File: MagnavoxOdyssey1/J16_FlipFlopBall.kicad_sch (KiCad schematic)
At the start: 15 parts

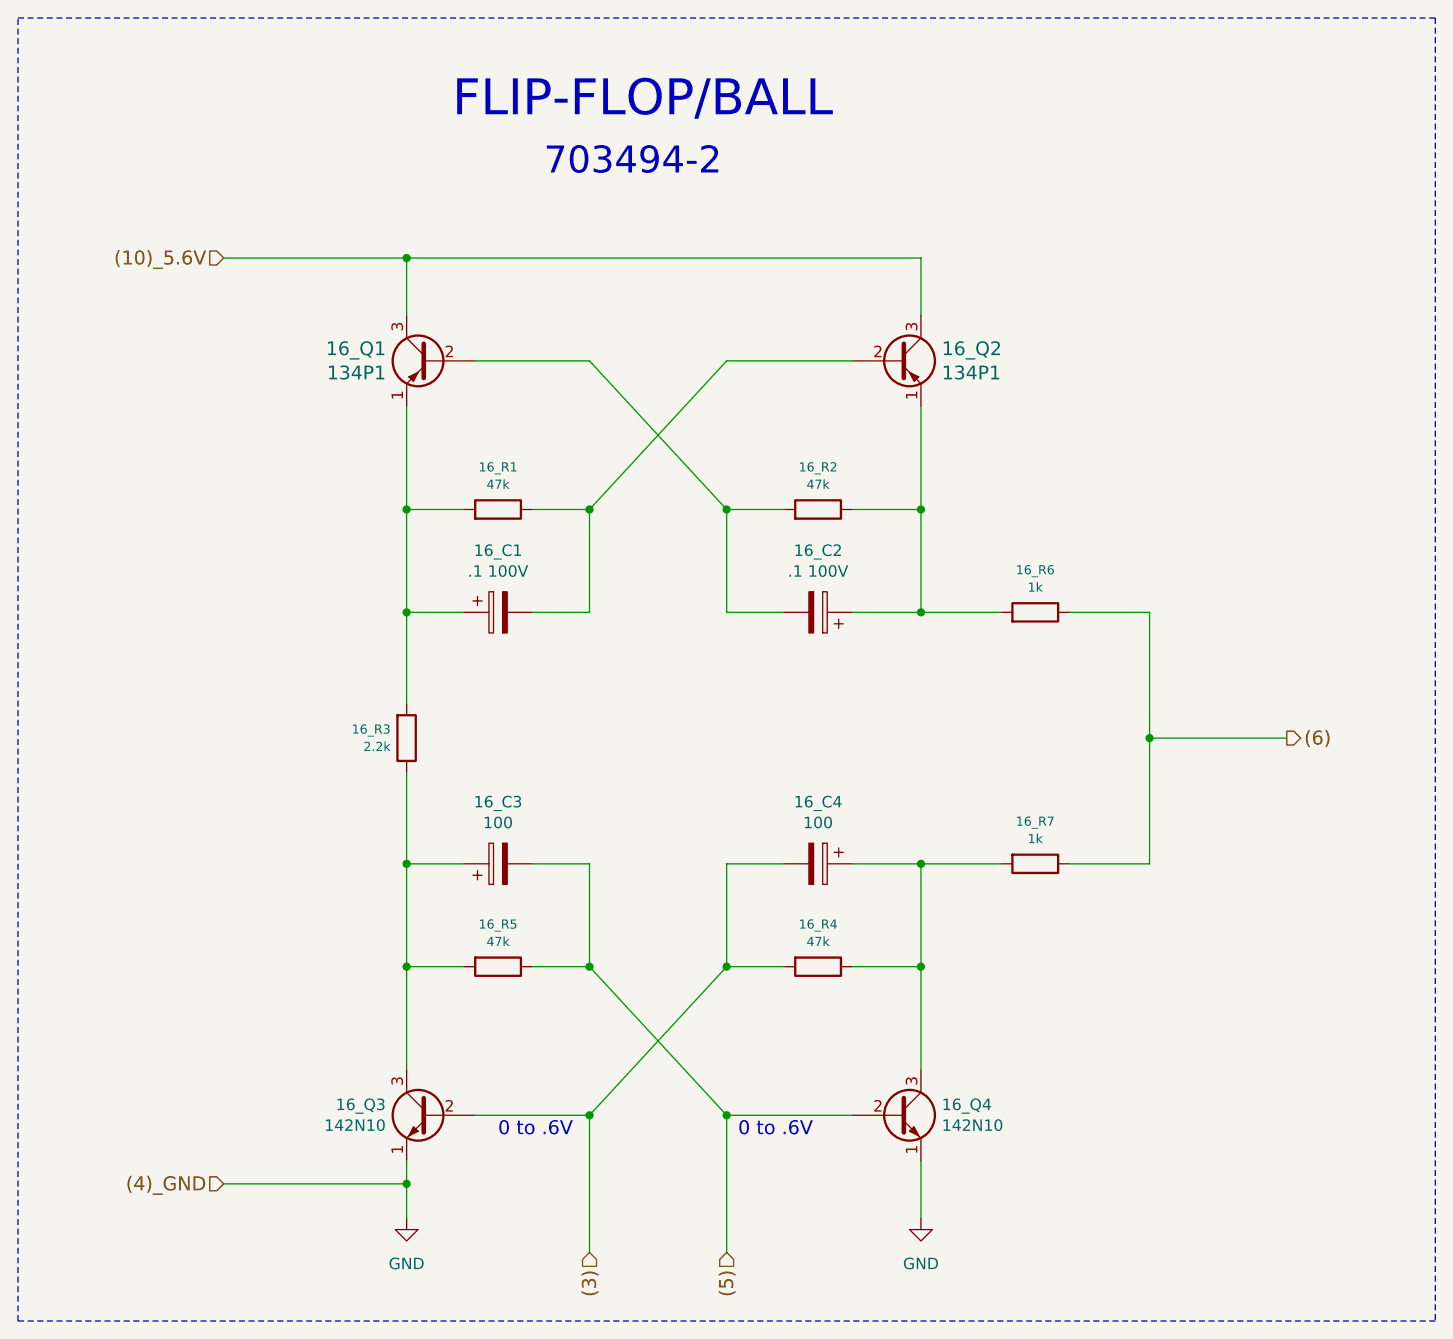
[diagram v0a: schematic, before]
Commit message: update to kicad 9
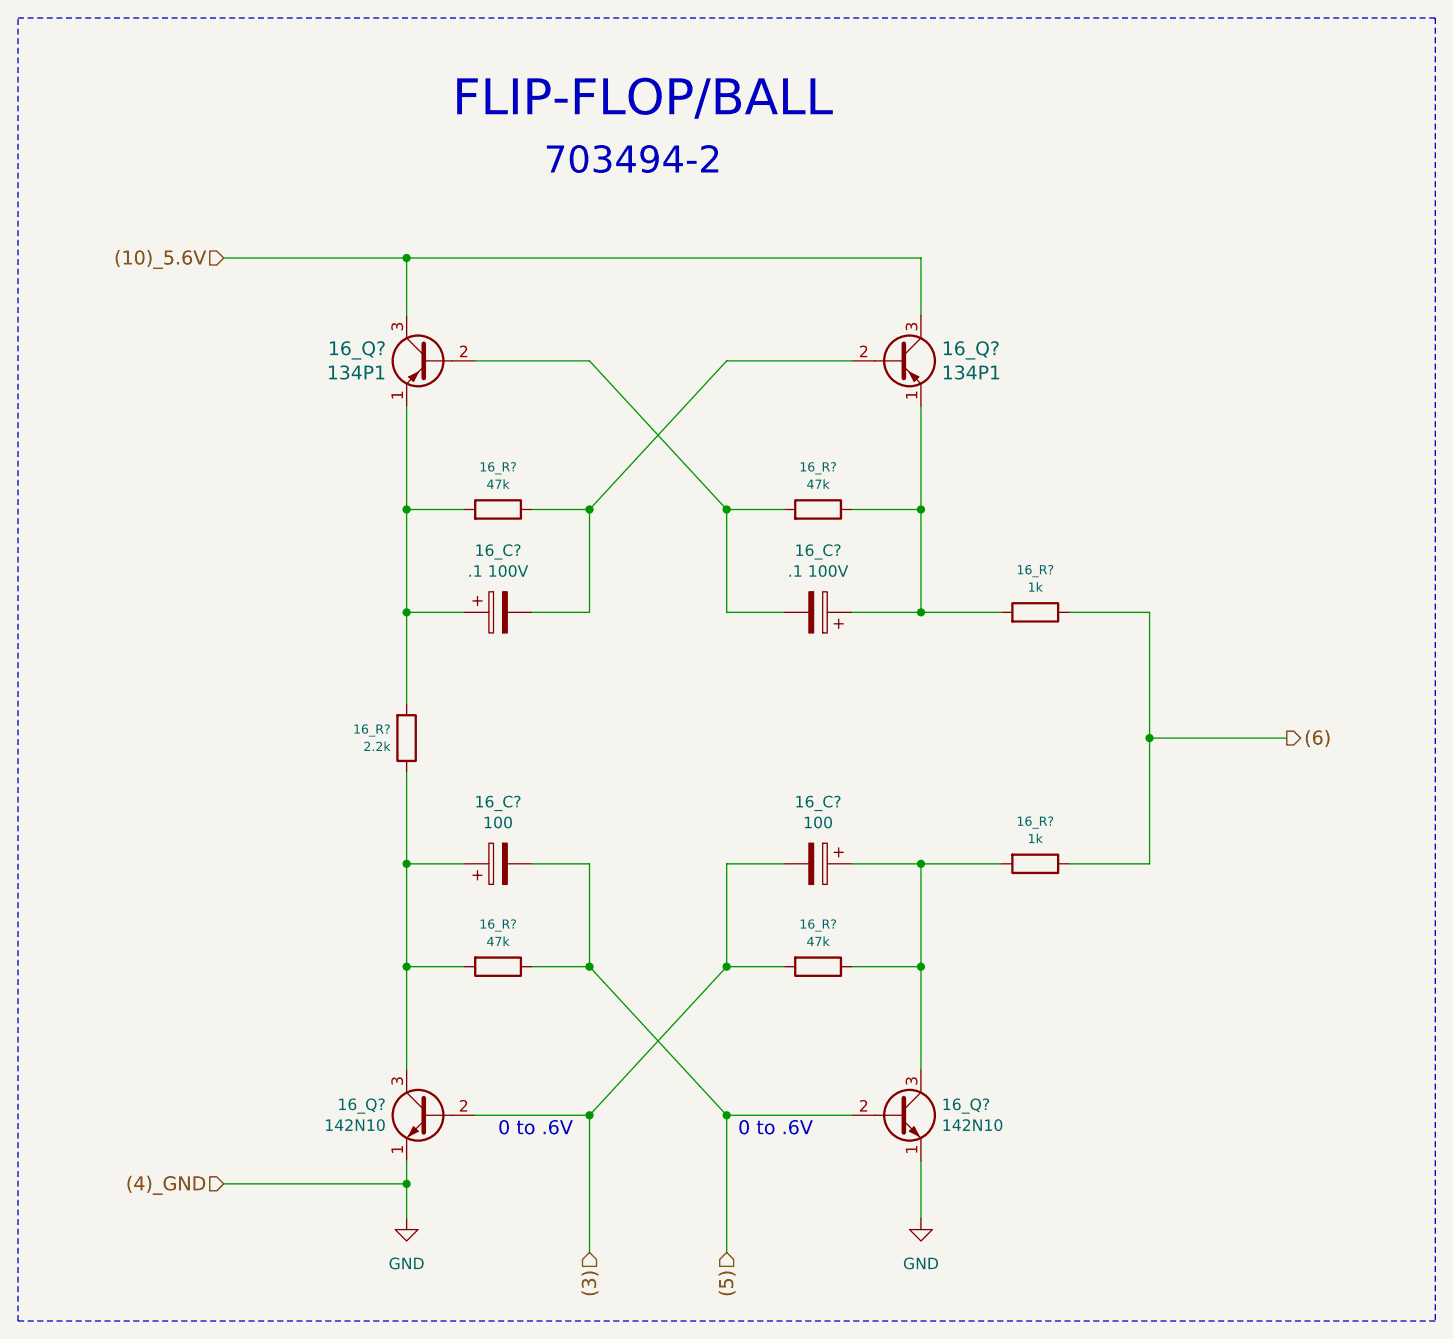
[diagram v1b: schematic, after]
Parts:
- 16_Q?: renamed from 16_Q4; symbol Device:Q_NPN_EBC -> Transistor_BJT:Q_NPN_EBC
- 16_Q?: renamed from 16_Q3; symbol Device:Q_NPN_EBC -> Transistor_BJT:Q_NPN_EBC
- 16_Q?: renamed from 16_Q2; symbol Device:Q_PNP_EBC -> Transistor_BJT:Q_PNP_EBC
- 16_Q?: renamed from 16_Q1; symbol Device:Q_PNP_EBC -> Transistor_BJT:Q_PNP_EBC
- renumbered 16_C3 to 16_C?, 16_C4 to 16_C?, 16_C1 to 16_C?, 16_C2 to 16_C?, 16_R4 to 16_R?, 16_R5 to 16_R?, 16_R7 to 16_R?, 16_R2 to 16_R?, 16_R1 to 16_R?, 16_R6 to 16_R?, 16_R3 to 16_R?
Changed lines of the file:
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@@
 (kicad_sch
-	(version 20231120)
+	(version 20250114)
 	(generator "eeschema")
-	(generator_version "8.0")
+	(generator_version "9.0")
 	(paper "A4")
+	(text "0 to .6V"
+		(exclude_from_sim no)
+		(at 116.84 140.97 0)
+		(effects
+			(font
+				(size 1.5494 1.5494)
+			)
+			(justify left bottom)
+		)
+	)
+	(text "0 to .6V"
+		(exclude_from_sim no)
+		(at 143.51 140.97 0)
+		(effects
+			(font
+				(size 1.5494 1.5494)
+			)
+			(justify left bottom)
+		)
+	)
+	(text "FLIP-FLOP/BALL"
+		(exclude_from_sim no)
+		(at 111.76 27.94 0)
+		(effects
+			(font
+				(size 3.9878 3.9878)
+			)
+			(justify left bottom)
+		)
+	)
+	(text "703494-2"
+		(exclude_from_sim no)
+		(at 121.92 34.29 0)
+		(effects
+			(font
+				(size 2.9972 2.9972)
+			)
+			(justify left bottom)
+		)
+	)
 	(junction
 		(at 142.24 71.12)
@@
 			(width 0)
 			(type default)
-		)
-	)
-	(text "0 to .6V"
-		(exclude_from_sim no)
-		(at 116.84 140.97 0)
-		(effects
-			(font
-				(size 1.5494 1.5494)
-			)
-			(justify left bottom)
-		)
-	)
-	(text "0 to .6V"
-		(exclude_from_sim no)
-		(at 143.51 140.97 0)
-		(effects
-			(font
-				(size 1.5494 1.5494)
-			)
-			(justify left bottom)
-		)
-	)
-	(text "FLIP-FLOP/BALL"
-		(exclude_from_sim no)
-		(at 111.76 27.94 0)
-		(effects
-			(font
-				(size 3.9878 3.9878)
-			)
-			(justify left bottom)
-		)
-	)
-	(text "703494-2"
-		(exclude_from_sim no)
-		(at 121.92 34.29 0)
-		(effects
-			(font
-				(size 2.9972 2.9972)
-			)
-			(justify left bottom)
 		)
 	)
@@
 	)
 	(symbol
-		(lib_id "Device:Q_NPN_EBC")
+		(lib_id "Transistor_BJT:Q_NPN_EBC")
 		(at 161.29 138.43 0)
 		(unit 1)
@@
 		(on_board yes)
 		(dnp no)
-		(property "Reference" "16_Q4"
+		(property "Reference" "16_Q?"
 			(at 166.1414 137.2616 0)
 			(effects
@@
 		(pin "3"
 		)
+		(instances
+			(project "MagnavoxOdyssey1"
+				(path "/adb6e295-eae5-402e-a614-02a705c3e27c/00000000-0000-0000-0000-0000588fbf2a"
+					(reference "16_Q?")
+					(unit 1)
+				)
+			)
+		)
 	)
 	(symbol
-		(lib_id "Device:Q_NPN_EBC")
+		(lib_id "Transistor_BJT:Q_NPN_EBC")
 		(at 109.22 138.43 0)
 		(mirror y)
@@
 		(on_board yes)
 		(dnp no)
-		(property "Reference" "16_Q3"
+		(property "Reference" "16_Q?"
 			(at 104.3686 137.2616 0)
 			(effects
@@
 		)
 		(pin "3"
+		)
+		(instances
+			(project "MagnavoxOdyssey1"
+				(path "/adb6e295-eae5-402e-a614-02a705c3e27c/00000000-0000-0000-0000-0000588fbf2a"
+					(reference "16_Q?")
+					(unit 1)
+				)
+			)
 		)
 	)
@@
 		(on_board yes)
 		(dnp no)
-		(property "Reference" "16_R4"
+		(property "Reference" "16_R?"
 			(at 152.4 117.221 90)
 			(effects
@@
 		)
 		(pin "2"
+		)
+		(instances
+			(project "MagnavoxOdyssey1"
+				(path "/adb6e295-eae5-402e-a614-02a705c3e27c/00000000-0000-0000-0000-0000588fbf2a"
+					(reference "16_R?")
+					(unit 1)
+				)
+			)
 		)
 	)
@@
 		(on_board yes)
 		(dnp no)
-		(property "Reference" "16_R5"
+		(property "Reference" "16_R?"
 			(at 116.84 117.221 90)
 			(effects
@@
 		)
 		(pin "2"
+		)
+		(instances
+			(project "MagnavoxOdyssey1"
+				(path "/adb6e295-eae5-402e-a614-02a705c3e27c/00000000-0000-0000-0000-0000588fbf2a"
+					(reference "16_R?")
+					(unit 1)
+				)
+			)
 		)
 	)
@@
 		(on_board yes)
 		(dnp no)
-		(property "Reference" "16_C3"
+		(property "Reference" "16_C?"
 			(at 116.84 103.632 90)
 			(effects
@@
 		)
 		(pin "2"
+		)
+		(instances
+			(project "MagnavoxOdyssey1"
+				(path "/adb6e295-eae5-402e-a614-02a705c3e27c/00000000-0000-0000-0000-0000588fbf2a"
+					(reference "16_C?")
+					(unit 1)
+				)
+			)
 		)
 	)
@@
 		(on_board yes)
 		(dnp no)
-		(property "Reference" "16_C4"
+		(property "Reference" "16_C?"
 			(at 152.4 103.632 90)
 			(effects
@@
 		)
 		(pin "2"
+		)
+		(instances
+			(project "MagnavoxOdyssey1"
+				(path "/adb6e295-eae5-402e-a614-02a705c3e27c/00000000-0000-0000-0000-0000588fbf2a"
+					(reference "16_C?")
+					(unit 1)
+				)
+			)
 		)
 	)
@@
 		(on_board yes)
 		(dnp no)
-		(property "Reference" "16_R7"
+		(property "Reference" "16_R?"
 			(at 176.53 105.791 90)
 			(effects
@@
 		)
 		(pin "1"
+		)
+		(instances
+			(project "MagnavoxOdyssey1"
+				(path "/adb6e295-eae5-402e-a614-02a705c3e27c/00000000-0000-0000-0000-0000588fbf2a"
+					(reference "16_R?")
+					(unit 1)
+				)
+			)
 		)
 	)
@@
 		(on_board yes)
 		(dnp no)
-		(property "Reference" "16_R2"
+		(property "Reference" "16_R?"
 			(at 152.4 66.421 90)
 			(effects
@@
 		)
 		(pin "2"
+		)
+		(instances
+			(project "MagnavoxOdyssey1"
+				(path "/adb6e295-eae5-402e-a614-02a705c3e27c/00000000-0000-0000-0000-0000588fbf2a"
+					(reference "16_R?")
+					(unit 1)
+				)
+			)
 		)
 	)
@@
 		(on_board yes)
 		(dnp no)
-		(property "Reference" "16_R1"
+		(property "Reference" "16_R?"
 			(at 116.84 66.421 90)
 			(effects
@@
 		)
 		(pin "2"
+		)
+		(instances
+			(project "MagnavoxOdyssey1"
+				(path "/adb6e295-eae5-402e-a614-02a705c3e27c/00000000-0000-0000-0000-0000588fbf2a"
+					(reference "16_R?")
+					(unit 1)
+				)
+			)
 		)
 	)
@@
 		(on_board yes)
 		(dnp no)
-		(property "Reference" "16_C1"
+		(property "Reference" "16_C?"
 			(at 116.84 75.692 90)
 			(effects
@@
 		)
 		(pin "2"
+		)
+		(instances
+			(project "MagnavoxOdyssey1"
+				(path "/adb6e295-eae5-402e-a614-02a705c3e27c/00000000-0000-0000-0000-0000588fbf2a"
+					(reference "16_C?")
+					(unit 1)
+				)
+			)
 		)
 	)
@@
 		(on_board yes)
 		(dnp no)
-		(property "Reference" "16_C2"
+		(property "Reference" "16_C?"
 			(at 152.4 75.692 90)
 			(effects
@@
 		)
 		(pin "2"
+		)
+		(instances
+			(project "MagnavoxOdyssey1"
+				(path "/adb6e295-eae5-402e-a614-02a705c3e27c/00000000-0000-0000-0000-0000588fbf2a"
+					(reference "16_C?")
+					(unit 1)
+				)
+			)
 		)
 	)
@@
 		(on_board yes)
 		(dnp no)
-		(property "Reference" "16_R6"
+		(property "Reference" "16_R?"
 			(at 176.53 77.851 90)
 			(effects
@@
 		)
 		(pin "2"
+		)
+		(instances
+			(project "MagnavoxOdyssey1"
+				(path "/adb6e295-eae5-402e-a614-02a705c3e27c/00000000-0000-0000-0000-0000588fbf2a"
+					(reference "16_R?")
+					(unit 1)
+				)
+			)
 		)
 	)
@@
 		(on_board yes)
 		(dnp no)
-		(property "Reference" "16_R3"
+		(property "Reference" "16_R?"
 			(at 104.902 95.5548 0)
 			(effects
@@
 		(pin "2"
 		)
+		(instances
+			(project "MagnavoxOdyssey1"
+				(path "/adb6e295-eae5-402e-a614-02a705c3e27c/00000000-0000-0000-0000-0000588fbf2a"
+					(reference "16_R?")
+					(unit 1)
+				)
+			)
+		)
 	)
 	(symbol
-		(lib_id "Device:Q_PNP_EBC")
+		(lib_id "Transistor_BJT:Q_PNP_EBC")
 		(at 161.29 54.61 0)
 		(unit 1)
@@
 		(on_board yes)
 		(dnp no)
-		(property "Reference" "16_Q2"
+		(property "Reference" "16_Q?"
 			(at 166.1414 53.2638 0)
 			(effects
@@
 		(pin "3"
 		)
+		(instances
+			(project "MagnavoxOdyssey1"
+				(path "/adb6e295-eae5-402e-a614-02a705c3e27c/00000000-0000-0000-0000-0000588fbf2a"
+					(reference "16_Q?")
+					(unit 1)
+				)
+			)
+		)
 	)
 	(symbol
-		(lib_id "Device:Q_PNP_EBC")
+		(lib_id "Transistor_BJT:Q_PNP_EBC")
 		(at 109.22 54.61 0)
 		(mirror y)
@@
 		(on_board yes)
 		(dnp no)
-		(property "Reference" "16_Q1"
+		(property "Reference" "16_Q?"
 			(at 104.394 53.2638 0)
 			(effects
@@
 		(pin "3"
 		)
-	)
+		(instances
+			(project "MagnavoxOdyssey1"
+				(path "/adb6e295-eae5-402e-a614-02a705c3e27c/00000000-0000-0000-0000-0000588fbf2a"
+					(reference "16_Q?")
+					(unit 1)
+				)
+			)
+		)
+	)

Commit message: annotate
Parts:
- gave numbers to parts that had none: 15
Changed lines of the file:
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@@
 		(on_board yes)
 		(dnp no)
-		(property "Reference" "16_Q?"
+		(property "Reference" "16_Q4"
 			(at 166.1414 137.2616 0)
 			(effects
@@
 			(project "MagnavoxOdyssey1"
 				(path "/adb6e295-eae5-402e-a614-02a705c3e27c/00000000-0000-0000-0000-0000588fbf2a"
-					(reference "16_Q?")
+					(reference "16_Q4")
 					(unit 1)
 				)
@@
 		(on_board yes)
 		(dnp no)
-		(property "Reference" "16_Q?"
+		(property "Reference" "16_Q3"
 			(at 104.3686 137.2616 0)
 			(effects
@@
 			(project "MagnavoxOdyssey1"
 				(path "/adb6e295-eae5-402e-a614-02a705c3e27c/00000000-0000-0000-0000-0000588fbf2a"
-					(reference "16_Q?")
+					(reference "16_Q3")
 					(unit 1)
 				)
@@
 		(on_board yes)
 		(dnp no)
-		(property "Reference" "16_R?"
+		(property "Reference" "16_R7"
 			(at 152.4 117.221 90)
 			(effects
@@
 			(project "MagnavoxOdyssey1"
 				(path "/adb6e295-eae5-402e-a614-02a705c3e27c/00000000-0000-0000-0000-0000588fbf2a"
-					(reference "16_R?")
+					(reference "16_R7")
 					(unit 1)
 				)
@@
 		(on_board yes)
 		(dnp no)
-		(property "Reference" "16_R?"
+		(property "Reference" "16_R6"
 			(at 116.84 117.221 90)
 			(effects
@@
 			(project "MagnavoxOdyssey1"
 				(path "/adb6e295-eae5-402e-a614-02a705c3e27c/00000000-0000-0000-0000-0000588fbf2a"
-					(reference "16_R?")
+					(reference "16_R6")
 					(unit 1)
 				)
@@
 		(on_board yes)
 		(dnp no)
-		(property "Reference" "16_C?"
+		(property "Reference" "16_C3"
 			(at 116.84 103.632 90)
 			(effects
@@
 			(project "MagnavoxOdyssey1"
 				(path "/adb6e295-eae5-402e-a614-02a705c3e27c/00000000-0000-0000-0000-0000588fbf2a"
-					(reference "16_C?")
+					(reference "16_C3")
 					(unit 1)
 				)
@@
 		(on_board yes)
 		(dnp no)
-		(property "Reference" "16_C?"
+		(property "Reference" "16_C4"
 			(at 152.4 103.632 90)
 			(effects
@@
 			(project "MagnavoxOdyssey1"
 				(path "/adb6e295-eae5-402e-a614-02a705c3e27c/00000000-0000-0000-0000-0000588fbf2a"
-					(reference "16_C?")
+					(reference "16_C4")
 					(unit 1)
 				)
@@
 		(on_board yes)
 		(dnp no)
-		(property "Reference" "16_R?"
+		(property "Reference" "16_R5"
 			(at 176.53 105.791 90)
 			(effects
@@
 			(project "MagnavoxOdyssey1"
 				(path "/adb6e295-eae5-402e-a614-02a705c3e27c/00000000-0000-0000-0000-0000588fbf2a"
-					(reference "16_R?")
+					(reference "16_R5")
 					(unit 1)
 				)
@@
 		(on_board yes)
 		(dnp no)
-		(property "Reference" "16_R?"
+		(property "Reference" "16_R2"
 			(at 152.4 66.421 90)
 			(effects
@@
 			(project "MagnavoxOdyssey1"
 				(path "/adb6e295-eae5-402e-a614-02a705c3e27c/00000000-0000-0000-0000-0000588fbf2a"
-					(reference "16_R?")
+					(reference "16_R2")
 					(unit 1)
 				)
@@
 		(on_board yes)
 		(dnp no)
-		(property "Reference" "16_R?"
+		(property "Reference" "16_R1"
 			(at 116.84 66.421 90)
 			(effects
@@
 			(project "MagnavoxOdyssey1"
 				(path "/adb6e295-eae5-402e-a614-02a705c3e27c/00000000-0000-0000-0000-0000588fbf2a"
-					(reference "16_R?")
+					(reference "16_R1")
 					(unit 1)
 				)
@@
 		(on_board yes)
 		(dnp no)
-		(property "Reference" "16_C?"
+		(property "Reference" "16_C1"
 			(at 116.84 75.692 90)
 			(effects
@@
 			(project "MagnavoxOdyssey1"
 				(path "/adb6e295-eae5-402e-a614-02a705c3e27c/00000000-0000-0000-0000-0000588fbf2a"
-					(reference "16_C?")
+					(reference "16_C1")
 					(unit 1)
 				)
@@
 		(on_board yes)
 		(dnp no)
-		(property "Reference" "16_C?"
+		(property "Reference" "16_C2"
 			(at 152.4 75.692 90)
 			(effects
@@
 			(project "MagnavoxOdyssey1"
 				(path "/adb6e295-eae5-402e-a614-02a705c3e27c/00000000-0000-0000-0000-0000588fbf2a"
-					(reference "16_C?")
+					(reference "16_C2")
 					(unit 1)
 				)
@@
 		(on_board yes)
 		(dnp no)
-		(property "Reference" "16_R?"
+		(property "Reference" "16_R3"
 			(at 176.53 77.851 90)
 			(effects
@@
 			(project "MagnavoxOdyssey1"
 				(path "/adb6e295-eae5-402e-a614-02a705c3e27c/00000000-0000-0000-0000-0000588fbf2a"
-					(reference "16_R?")
+					(reference "16_R3")
 					(unit 1)
 				)
@@
 		(on_board yes)
 		(dnp no)
-		(property "Reference" "16_R?"
+		(property "Reference" "16_R4"
 			(at 104.902 95.5548 0)
 			(effects
@@
 			(project "MagnavoxOdyssey1"
 				(path "/adb6e295-eae5-402e-a614-02a705c3e27c/00000000-0000-0000-0000-0000588fbf2a"
-					(reference "16_R?")
+					(reference "16_R4")
 					(unit 1)
 				)
@@
 		(on_board yes)
 		(dnp no)
-		(property "Reference" "16_Q?"
+		(property "Reference" "16_Q2"
 			(at 166.1414 53.2638 0)
 			(effects
@@
 			(project "MagnavoxOdyssey1"
 				(path "/adb6e295-eae5-402e-a614-02a705c3e27c/00000000-0000-0000-0000-0000588fbf2a"
-					(reference "16_Q?")
+					(reference "16_Q2")
 					(unit 1)
 				)
@@
 		(on_board yes)
 		(dnp no)
-		(property "Reference" "16_Q?"
+		(property "Reference" "16_Q1"
 			(at 104.394 53.2638 0)
 			(effects
@@
 			(project "MagnavoxOdyssey1"
 				(path "/adb6e295-eae5-402e-a614-02a705c3e27c/00000000-0000-0000-0000-0000588fbf2a"
-					(reference "16_Q?")
-					(unit 1)
-				)
+					(reference "16_Q1")
+					(unit 1)
+				)
